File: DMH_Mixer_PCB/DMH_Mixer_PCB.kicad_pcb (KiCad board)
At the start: 2 copper layers, 48 x 138 mm, 51 parts, among them J0 Conn_01x01, J100 IDC_02x05, J200 IDC_02x05, J50 Conn_01x08, J60 Conn_01x08, SW1 SW_SPDT_321, SW2 SW_SPDT_321, SW3 SW_SPDT_321, SW4 SW_SPDT_321, U1 TL074

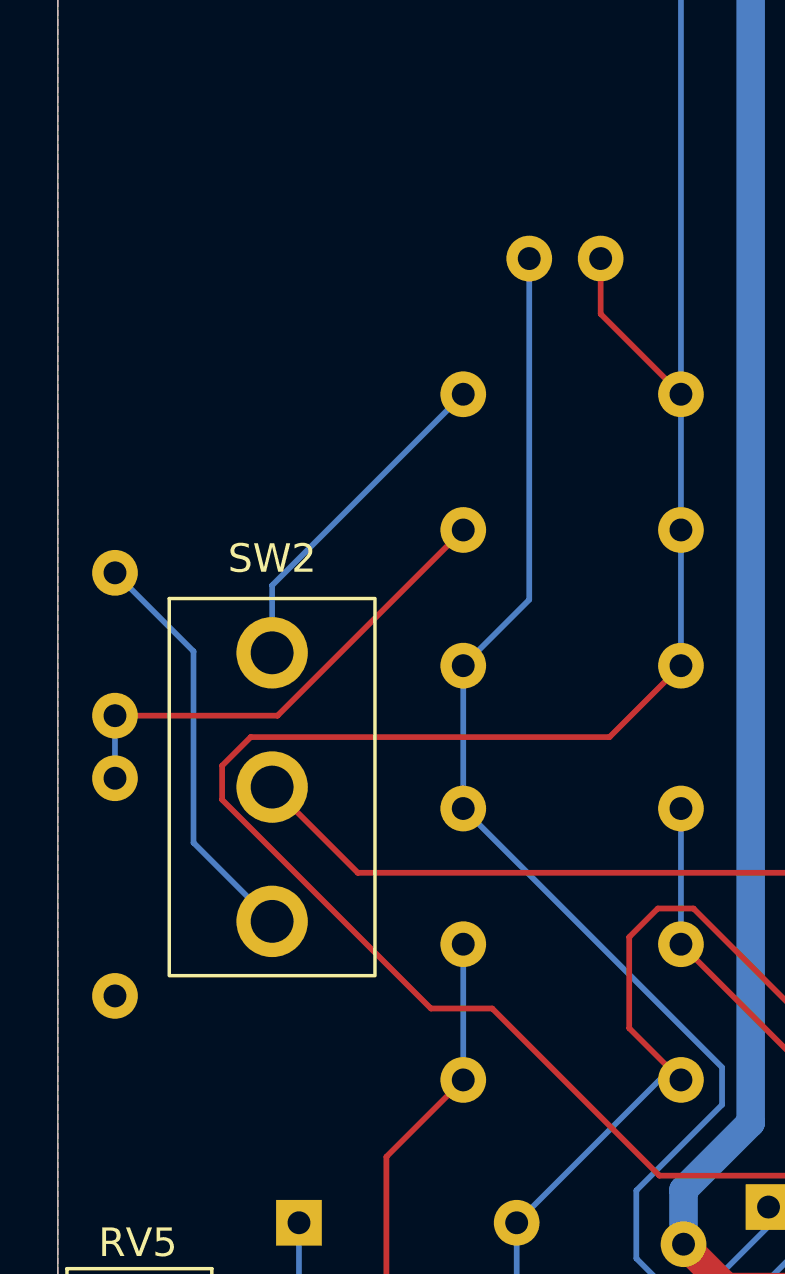
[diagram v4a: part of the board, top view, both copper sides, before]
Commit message: Added Zener limiting
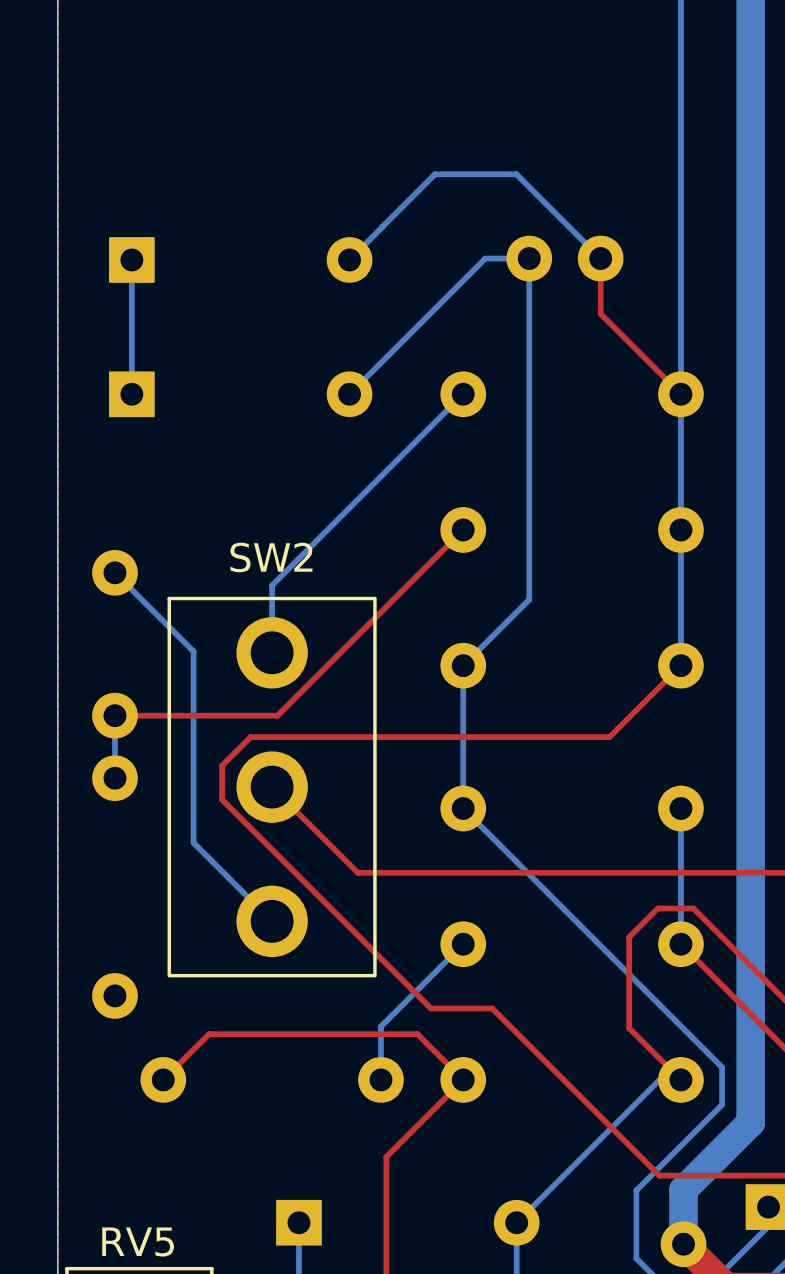
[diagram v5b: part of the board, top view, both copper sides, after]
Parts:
- added D3: ZPD3V3, Diode_THT:D_DO-35_SOD27_P7.62mm_Horizontal, B.Cu at (53.6, 80.5)
- added D6: ZPD3V3, Diode_THT:D_DO-35_SOD27_P7.62mm_Horizontal, B.Cu at (53.6, 75.8)
- added R21: 27k, Resistor_THT:R_Axial_DIN0207_L6.3mm_D2.5mm_P7.62mm_Horizontal, B.Cu at (62.3, 104.5)
- R2, R4, R6, R8: value 27k -> 22k
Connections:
- R15 pad 2: Net-(U1D-+) -> Net-(R15-Pad2)
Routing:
- net Net-(D6-A): track 141.2 -> 152.5 mm
- net Net-(D3-A): track 47.5 -> 55.8 mm
- net Net-(U1D-+): track 69.1 -> 76.2 mm
- net Net-(R15-Pad2): track 0.00 -> 5.94 mm
- net Net-(D3-K): track 0.00 -> 4.70 mm

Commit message: PCB redesign ongoing
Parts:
- removed D5: SB140+, Diode_THT:D_DO-41_SOD81_P10.16mm_Horizontal
- removed D6: ZPD3V3, Diode_THT:D_DO-35_SOD27_P7.62mm_Horizontal
- removed R14, R15, R17, R19: 100k, Resistor_THT:R_Axial_DIN0207_L6.3mm_D2.5mm_P7.62mm_Horizontal
- removed R16, R20: 1k, Resistor_THT:R_Axial_DIN0207_L6.3mm_D2.5mm_P7.62mm_Horizontal
- removed R18, R21: 27k, Resistor_THT:R_Axial_DIN0207_L6.3mm_D2.5mm_P7.62mm_Horizontal
- removed RV5: 20k, Potentiometer_THT:Potentiometer_Bourns_3296W_Vertical
- added REF**: CUI_MJ-63052A, SynthStuff:CUI_MJ-63052A, F.Cu at (75.0, 190.2)
- added REF**: CUI_MJ-63052A, SynthStuff:CUI_MJ-63052A, F.Cu at (91.5, 208.8)
- added REF**: CUI_MJ-63052A, SynthStuff:CUI_MJ-63052A, F.Cu at (75.0, 208.8)
- added SW5: SW_DPDT, SynthStuff:PinHeader_2x03_P2.54mm_Vertical_142536, F.Cu at (104.0, 160.2)
- D1: value 1N4148 -> SB140+; footprint Diode_THT:D_DO-35_SOD27_P7.62mm_Horizontal -> Diode_THT:D_DO-41_SOD81_P10.16mm_Horizontal
- D2: value 1N4148 -> SB140-; footprint Diode_THT:D_DO-35_SOD27_P7.62mm_Horizontal -> Diode_THT:D_DO-41_SOD81_P10.16mm_Horizontal
- D3: value ZPD3V3 -> ZPD3V9
- D4: value SB140- -> ZPD3V9; footprint Diode_THT:D_DO-41_SOD81_P10.16mm_Horizontal -> Diode_THT:D_DO-35_SOD27_P7.62mm_Horizontal
- R13: value 100k -> 1k
- U1: value TL074 -> TL072; footprint Package_DIP:DIP-14_W7.62mm_Socket -> Package_DIP:DIP-8_W7.62mm_Socket
- moved R6 44.2 mm to (108.9, 137.0)
- moved R5 42.9 mm to (107.6, 131.5)
- moved R4 40.1 mm to (105.1, 88.5)
- moved R13 39.4 mm to (112.1, 93.0)
- moved R3 37.7 mm to (102.9, 81.5)
- moved R8 37.0 mm to (36.1, 154.0)
- moved R1 32.6 mm to (32.7, 56.5)
- moved R2 29.1 mm to (38.9, 46.0)
- moved C11 25.3 mm to (44.8, 74.0)
- moved D1 22.5 mm to (37.2, 113.0)
- moved D2 20.9 mm to (46.6, 119.5)
- moved R7 17.1 mm to (45.5, 152.1)
- moved D3 15.4 mm to (38.2, 81.2)
- moved R11 14.8 mm to (38.8, 142.8)
- moved C12 14.5 mm to (105.8, 102.8)
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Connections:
- C11 pad 1: Net-(D6-A) -> Net-(D3-A)
- C11 pad 2: Net-(D3-A) -> Net-(D4-A)
- C12 pad 2: Net-(U1D-+) -> Net-(C12-Pad2)
- C4 pad 1: +12V -> GND
- C4 pad 2: GND -> -12V
- C5 pad 1: GND -> +12V
- C5 pad 2: -12V -> GND
- D1 pad 1: Net-(D1-K) -> +12V
- D2 pad 1: Net-(D1-A) -> Net-(D2-K)
- D2 pad 2: Net-(D1-K) -> -12V
- D4 pad 2: -12V -> Net-(D4-A)
- J100 pad 1a: Net-(D4-K) -> Net-(D2-K)
- J100 pad 1b: Net-(D4-K) -> Net-(D2-K)
- J100 pad 5a: Net-(D5-A) -> Net-(D1-A)
- J100 pad 5b: Net-(D5-A) -> Net-(D1-A)
- J200 pad 8: Net-(J200-Pin_8) -> unconnected-(J200-Pin_8-Pad8)
- J50 pad 5: /Core Circuit/Clipped Output -> /Core Circuit/Output
- J50 pad 6: /Core Circuit/Output -> unconnected-(J50-Pin_6-Pad6)
- J60 pad 6: Net-(J200-Pin_8) -> unconnected-(J60-Pin_6-Pad6)
- R1 pad 2: Net-(D6-A) -> Net-(D3-A)
- R10 pad 1: GND -> Net-(D4-A)
- R10 pad 2: Net-(C8-Pad2) -> Net-(U1B--)
- R11 pad 1: GND -> Net-(R11-Pad1)
- R11 pad 2: Net-(C9-Pad2) -> Net-(D4-A)
- R12 pad 1: GND -> Net-(U1B--)
- R12 pad 2: Net-(C10-Pad2) -> Net-(C12-Pad2)
- R13 pad 1: Net-(D6-A) -> Net-(C12-Pad2)
- R13 pad 2: Net-(D3-A) -> /Core Circuit/Output
- R2 pad 2: Net-(D6-A) -> Net-(D3-A)
- R3 pad 2: Net-(D6-A) -> Net-(D3-A)
- R4 pad 2: Net-(D6-A) -> Net-(D3-A)
- R5 pad 2: Net-(D6-A) -> Net-(D3-A)
- R6 pad 2: Net-(D6-A) -> Net-(D3-A)
- R7 pad 2: Net-(D6-A) -> Net-(D3-A)
- R8 pad 2: Net-(D6-A) -> Net-(D3-A)
- R9 pad 1: GND -> Net-(D3-A)
- R9 pad 2: Net-(C7-Pad2) -> Net-(D4-A)
- U1 pad 1: Net-(D3-A) -> Net-(D4-A)
- U1 pad 2: Net-(D6-A) -> Net-(D3-A)
- U1 pad 4: +12V -> -12V
- U1 pad 7: Net-(U1D-+) -> Net-(C12-Pad2)
- U1 pad 8: Net-(R19-Pad2) -> +12V
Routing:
- net Net-(D6-A): track 152.5 -> 0.00 mm
- net /Core Circuit/Input 1: track 117.4 -> 0.00 mm
- net +12V: track 89.9 -> 0.00 mm
- net /Core Circuit/Input 2: track 82.5 -> 0.00 mm
- net /Core Circuit/Output: track 79.0 -> 0.00 mm
- net Net-(U1D-+): track 76.2 -> 0.00 mm
- net -12V: track 58.0 -> 0.00 mm
- net Net-(D1-A): track 56.6 -> 0.00 mm
- net Net-(D3-A): track 55.8 -> 0.00 mm
- net Net-(R19-Pad2): track 48.7 -> 0.00 mm
- net /Core Circuit/Clipped Output: track 47.1 -> 0.00 mm
- net Net-(U1B--): track 43.1 -> 0.00 mm
- net /Core Circuit/Input 3: track 41.2 -> 0.00 mm
- net Net-(SW4-B): track 40.6 -> 0.00 mm
- net Net-(U1C--): track 36.0 -> 0.00 mm
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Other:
- board size 48 x 138 mm -> 48 x 156 mm

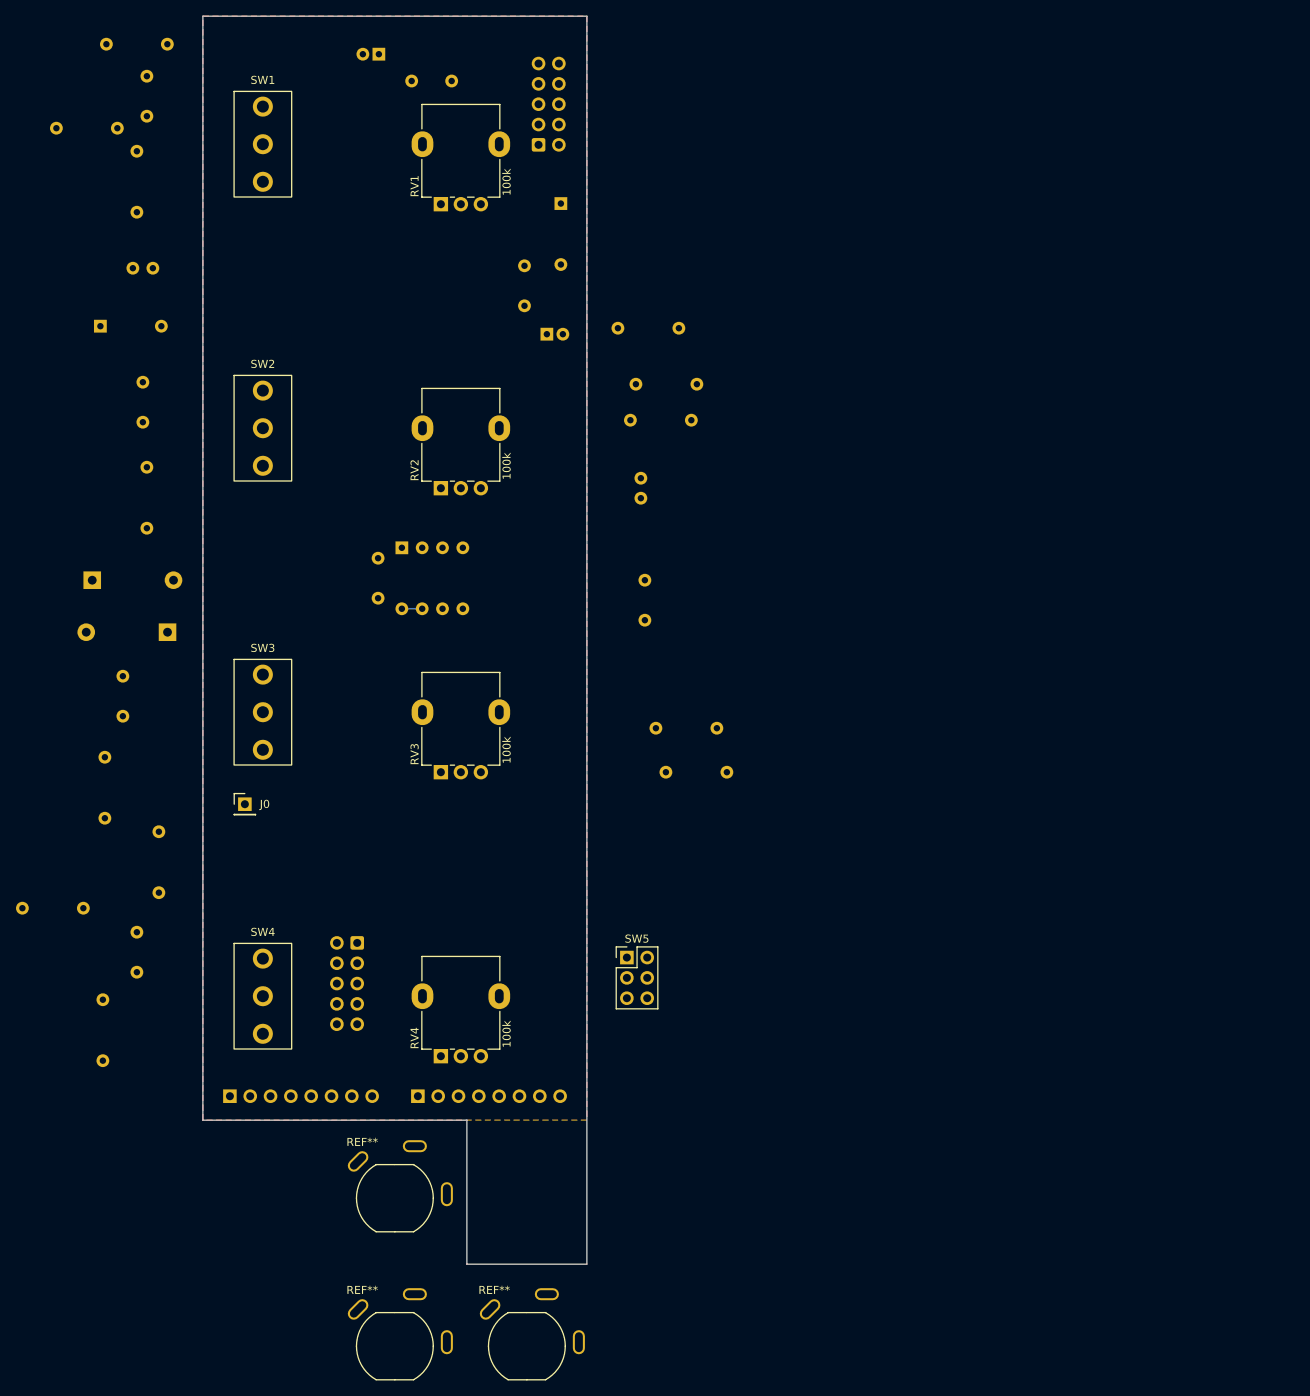
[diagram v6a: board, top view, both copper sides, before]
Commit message: PCB Component placement ready
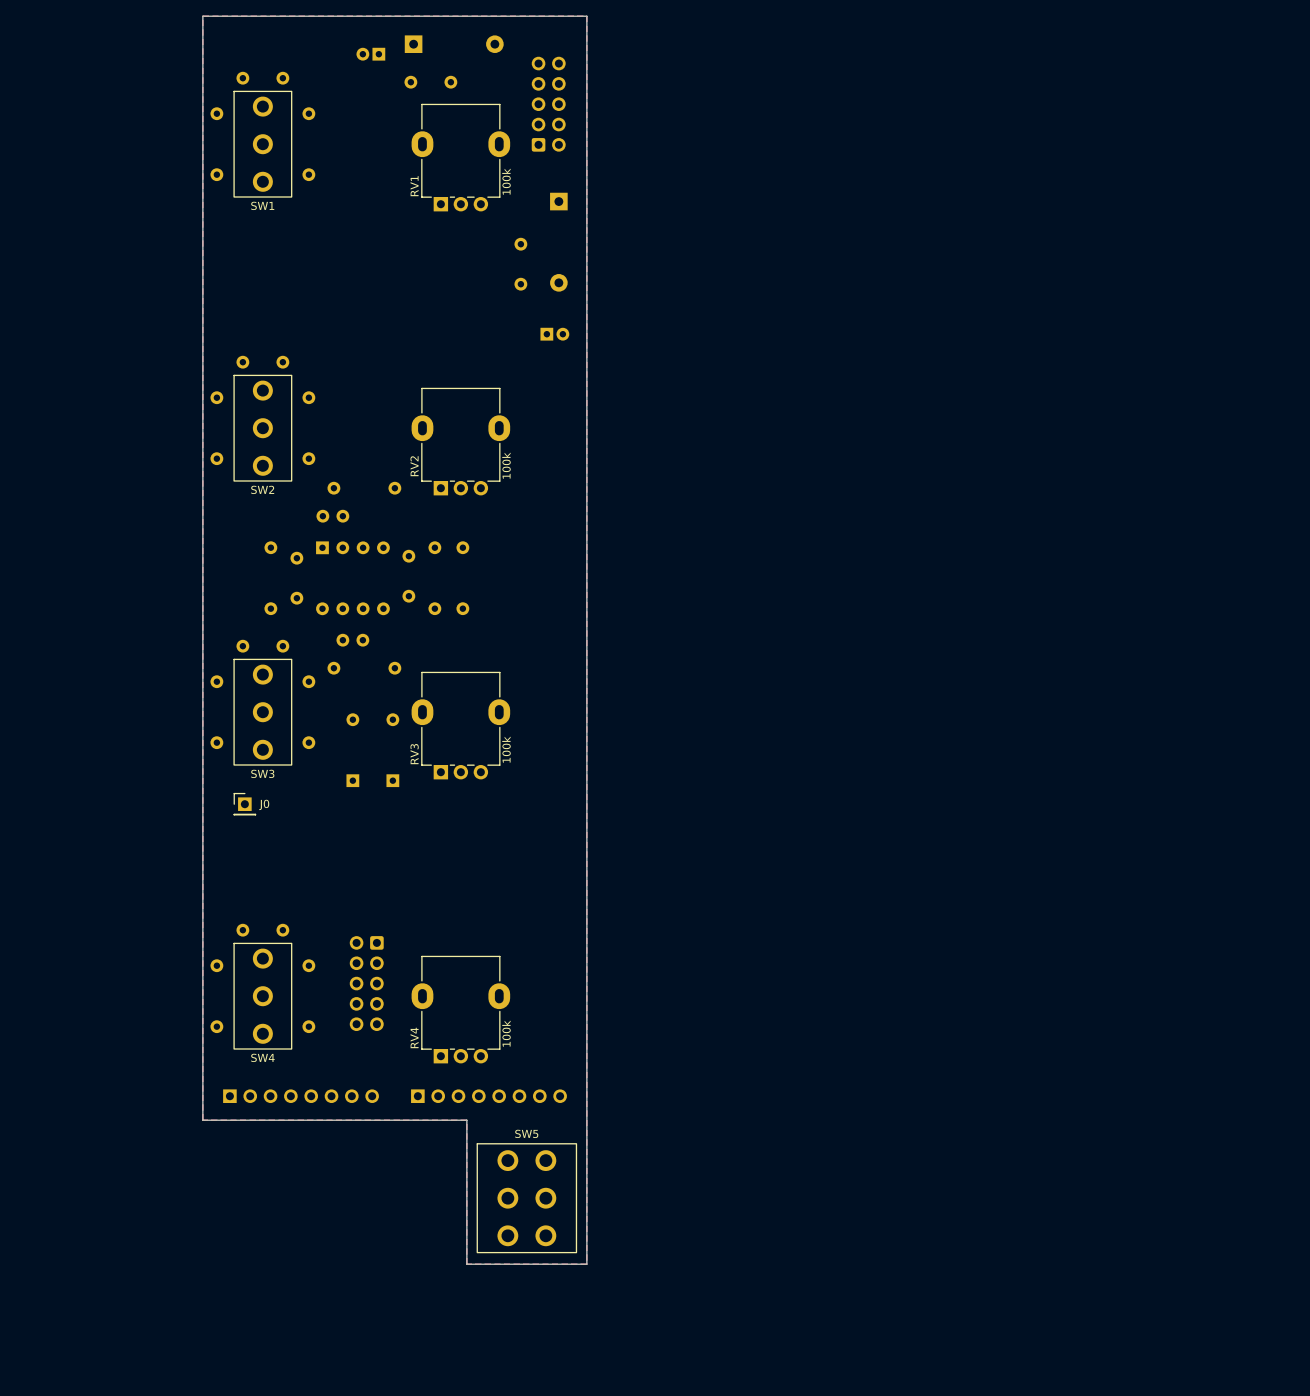
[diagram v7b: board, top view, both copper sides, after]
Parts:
- removed REF** (x3): CUI_MJ-63052A, SynthStuff:CUI_MJ-63052A
- SW5: footprint SynthStuff:PinHeader_2x03_P2.54mm_Vertical_142536 -> SynthStuff:Toggle_Switch_2_Poles_THT
- moved D1 78.1 mm to (77.3, 46.0)
- moved D4 75.1 mm to (74.8, 138.1), turned to 90 degrees
- moved D2 72.7 mm to (95.5, 65.7), turned to -90 degrees
- moved D3 65.0 mm to (69.8, 138.1), turned to 90 degrees
- moved R12 61.1 mm to (75.0, 124.0), turned to 180 degrees
- moved C3 59.6 mm to (77.0, 50.8), turned to 0 degrees
- moved R6 57.3 mm to (52.8, 125.7), turned to -90 degrees
- moved R4 52.4 mm to (52.8, 90.2), turned to -90 degrees
- moved R11 48.9 mm to (80.0, 116.6)
- moved R9 47.2 mm to (75.0, 101.5), turned to 180 degrees
- moved C5 46.3 mm to (62.8, 115.2)
- moved R5 43.8 mm to (64.2, 125.7), turned to -90 degrees
- moved R3 39.6 mm to (64.2, 90.2), turned to -90 degrees
- moved C11 39.1 mm to (68.5, 105.0)
- moved C12 39.0 mm to (71.0, 120.5), turned to 180 degrees
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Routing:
- net Net-(U1D--): track 2.54 -> 0.00 mm

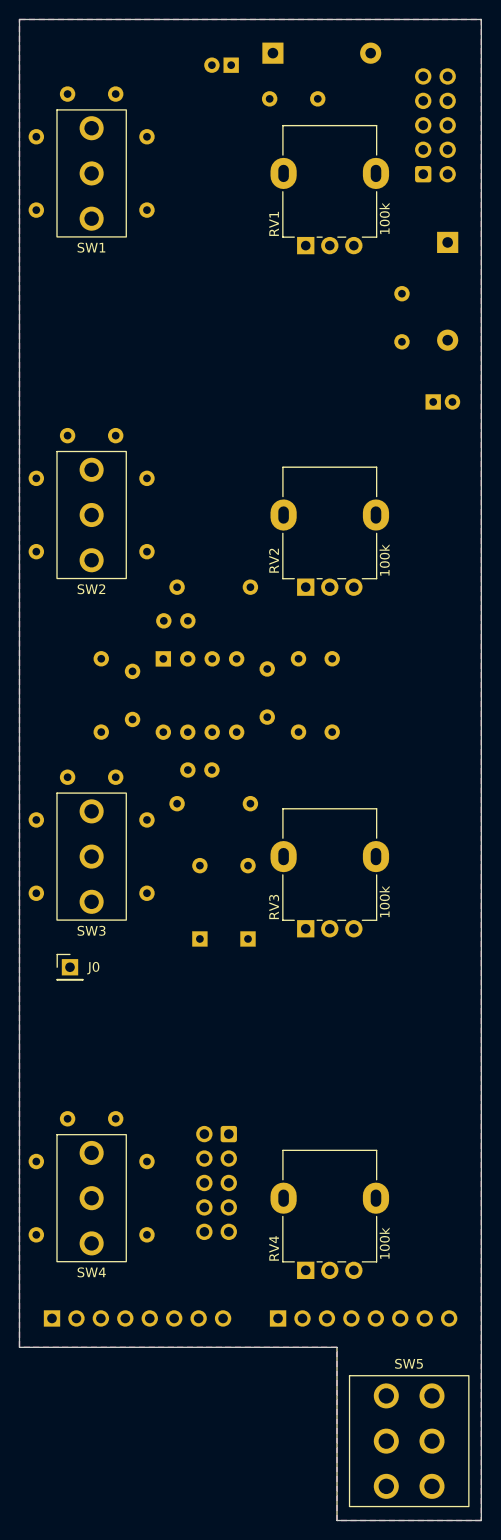
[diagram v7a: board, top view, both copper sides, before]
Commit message: Finished routing main PCB
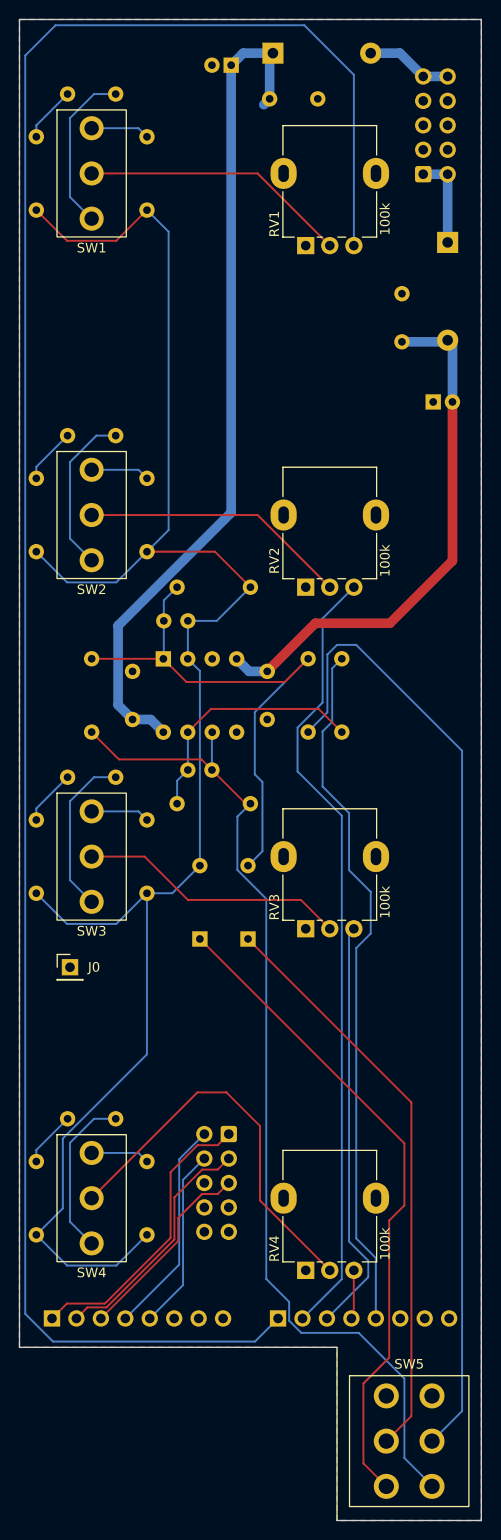
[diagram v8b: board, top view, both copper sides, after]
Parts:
- moved R10 1.00 mm to (58.5, 108.9)
- moved R11 1.00 mm to (81.0, 116.6)
- moved R13 1.00 mm to (84.5, 116.6)
- moved C6 0.25 mm to (76.8, 115.2)
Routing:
- net /Core Circuit/Input 1: track 0.00 -> 214.6 mm
- net Net-(D3-A): track 0.00 -> 187.1 mm
- net Net-(U1B--): track 0.00 -> 106.9 mm
- net Net-(R11-Pad1): track 0.00 -> 100.9 mm
- net +12V: track 0.00 -> 87.8 mm
- net /Core Circuit/Input 2: track 0.00 -> 82.0 mm
- net /Core Circuit/Output: track 0.00 -> 72.9 mm
- net Net-(D3-K): track 0.00 -> 68.4 mm
- net Net-(D4-K): track 0.00 -> 60.3 mm
- net Net-(D4-A): track 0.00 -> 57.3 mm
- net -12V: track 0.00 -> 55.7 mm
- net /Core Circuit/Input 3: track 0.00 -> 43.3 mm
- net Net-(SW4-B): track 0.00 -> 41.5 mm
- net Net-(J200-Pin_1): track 0.00 -> 30.3 mm
- net Net-(SW3-B): track 0.00 -> 27.9 mm
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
